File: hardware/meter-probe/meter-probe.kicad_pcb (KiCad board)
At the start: 2 copper layers, 38.9 x 72.6 mm, 22 parts, among them J1 Main Board, Q1 BSS138, SW1 Sensor Button, U1 RT9193, U2 TCS3472, U3 P82B96

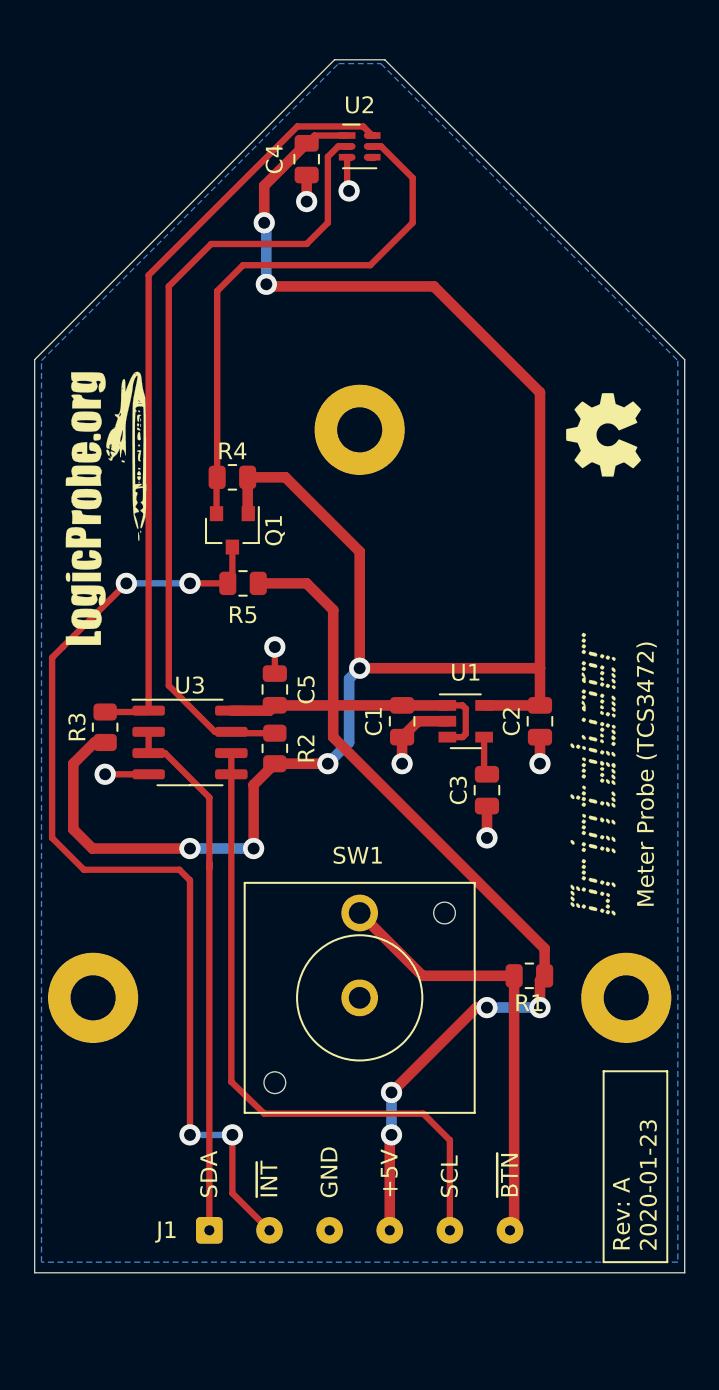
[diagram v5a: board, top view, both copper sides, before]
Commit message: Changed wire-to-board footprint for the meter probe
Created a footprint with more compact pin spacing, that includes
mechanical holes for attaching a cable tie that acts as a strain
relief for the cable.

Increased the length of the board, still within the package space,
to accommodate this change.
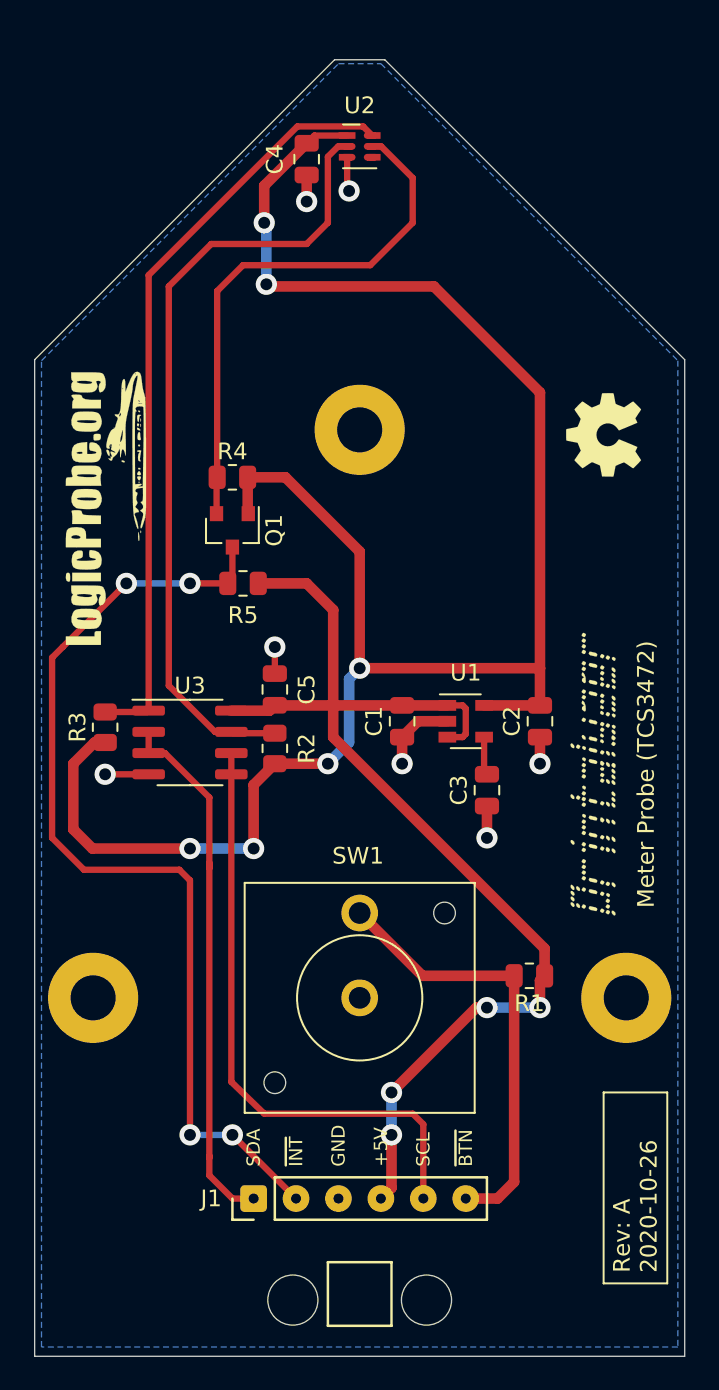
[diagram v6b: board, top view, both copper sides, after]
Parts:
- J1: footprint Connector_Wire:SolderWire-0.1sqmm_1x06_P3.6mm_D0.4mm_OD1mm -> lib_fp:SolderWire-0.1sqmm_1x06_Cable
- moved J1 9.20 mm to (120.7, 128.9)
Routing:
- net /SCL: track 39.6 -> 36.7 mm
- net +5V: track 70.6 -> 69.0 mm
- net /~INT: track 59.2 -> 57.9 mm
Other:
- board size 38.9 x 72.6 mm -> 38.9 x 77.6 mm
- board text added: "Rev: A 2020-10-26"
- board text removed: "Rev: A 2020-01-23"

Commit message: Updated PCB with component changes and tweaked the routing
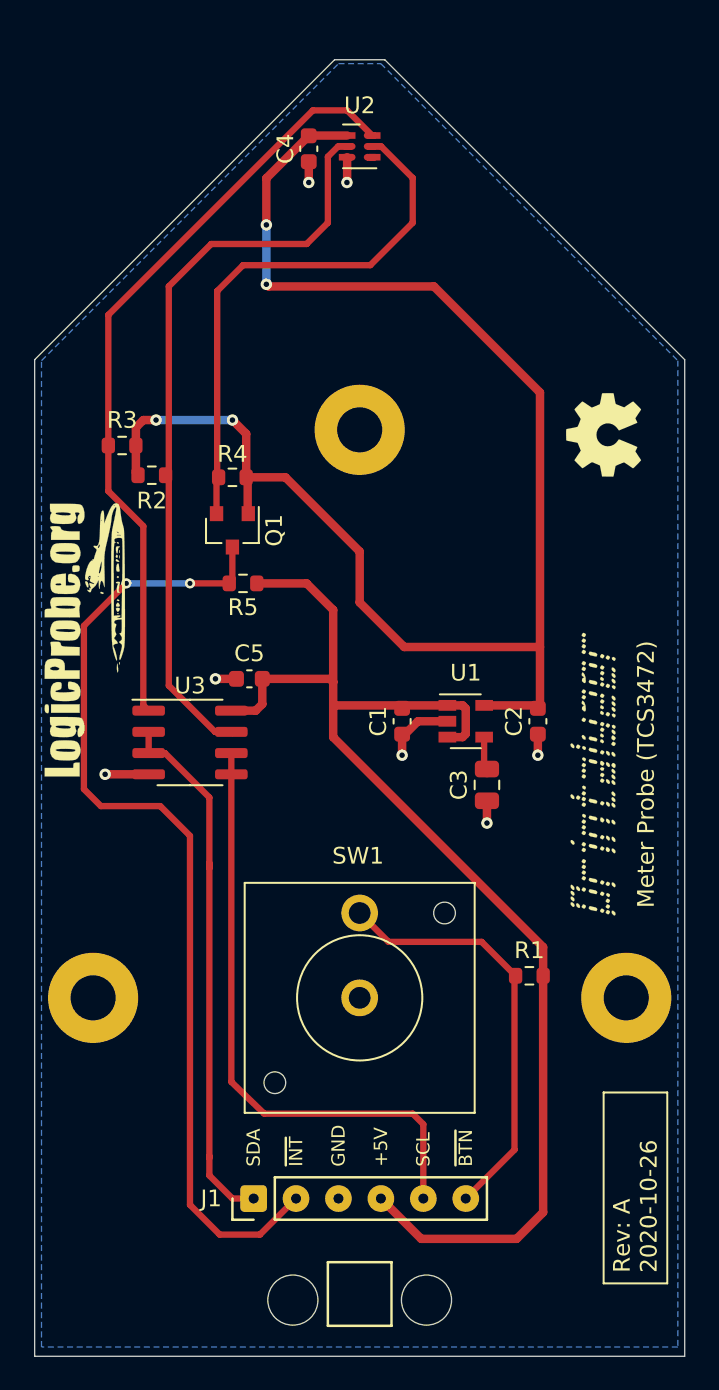
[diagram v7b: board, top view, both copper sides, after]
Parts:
- C1, C2, C4, C5: footprint Capacitor_SMD:C_0805_2012Metric -> Capacitor_SMD:C_0603_1608Metric
- R1, R2, R3, R4, R5: footprint Resistor_SMD:R_0805_2012Metric -> Resistor_SMD:R_0603_1608Metric
- moved R2 17.9 mm to (108.2, 85.6), turned to 0 degrees
- moved R3 16.9 mm to (106.4, 83.8), turned to 180 degrees
- moved G*** 7.98 mm to (104.1, 95.5)
- moved C5 1.65 mm to (114.0, 97.8), turned to 180 degrees
- moved C4 0.63 mm to (117.6, 66.1)
- moved C3 0.31 mm to (128.3, 104.1)
- moved C2 0.13 mm to (131.3, 100.3)
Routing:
- net +3V3: track 114.8 -> 92.1 mm, vias 6 -> 4
- net +5V: track 69.0 -> 76.4 mm, vias 4 -> 0
- net GND: track 16.0 -> 13.6 mm
- net Net-(R2-Pad2): track 47.9 -> 45.6 mm
- net /~INT: track 57.9 -> 59.3 mm, vias 4 -> 2
- net /~BUTTON: track 26.5 -> 25.5 mm
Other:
- net class Power added: clearance 0.1524, trace_width 0.508, via_dia 0.6858, via_drill 0.3302
- net class Signal added: clearance 0.1524, trace_width 0.381, via_dia 0.6096, via_drill 0.3048

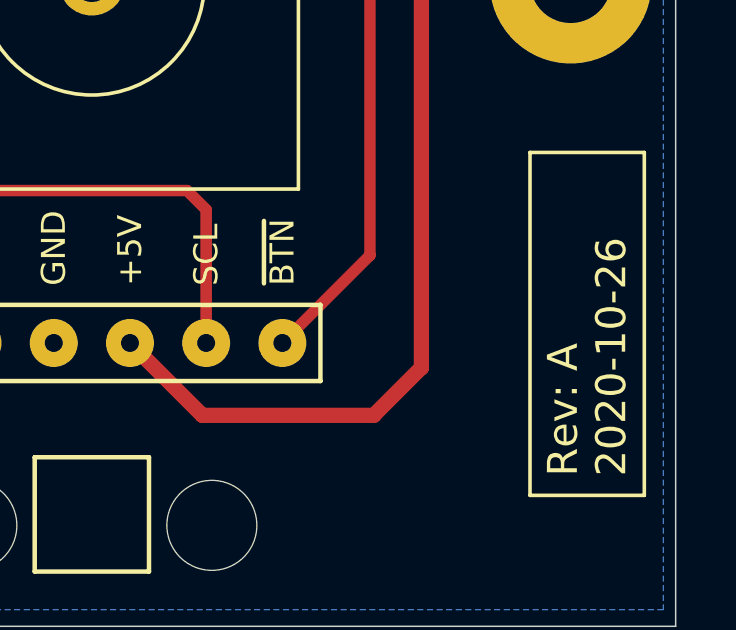
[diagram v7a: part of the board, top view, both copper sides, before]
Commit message: Added 10uF capacitor to +5V input on meter PCB
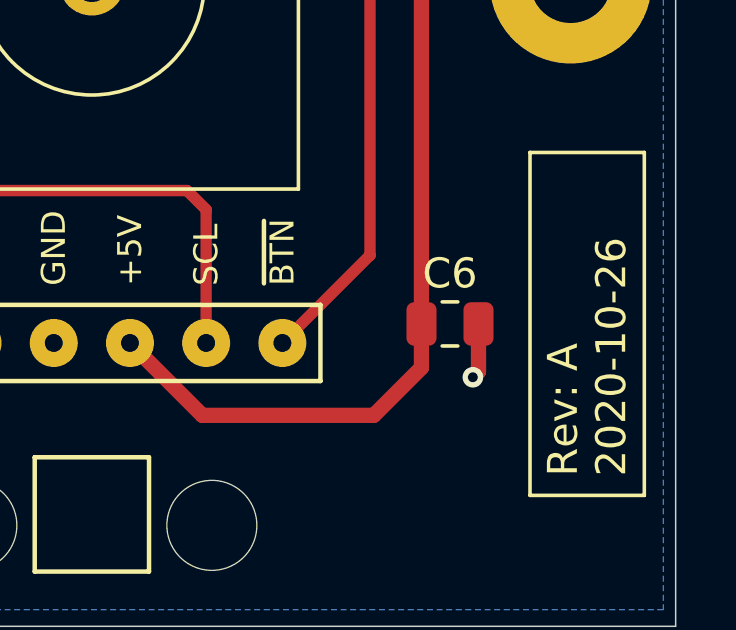
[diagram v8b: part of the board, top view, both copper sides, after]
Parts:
- added C6: 10uF, Capacitor_SMD:C_0805_2012Metric, F.Cu at (132.6, 128.3)
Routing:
- net GND: track 13.6 -> 15.4 mm, vias 7 -> 8
